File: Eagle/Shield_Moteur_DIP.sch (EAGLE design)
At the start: 25 parts, among them IC1 L6205N

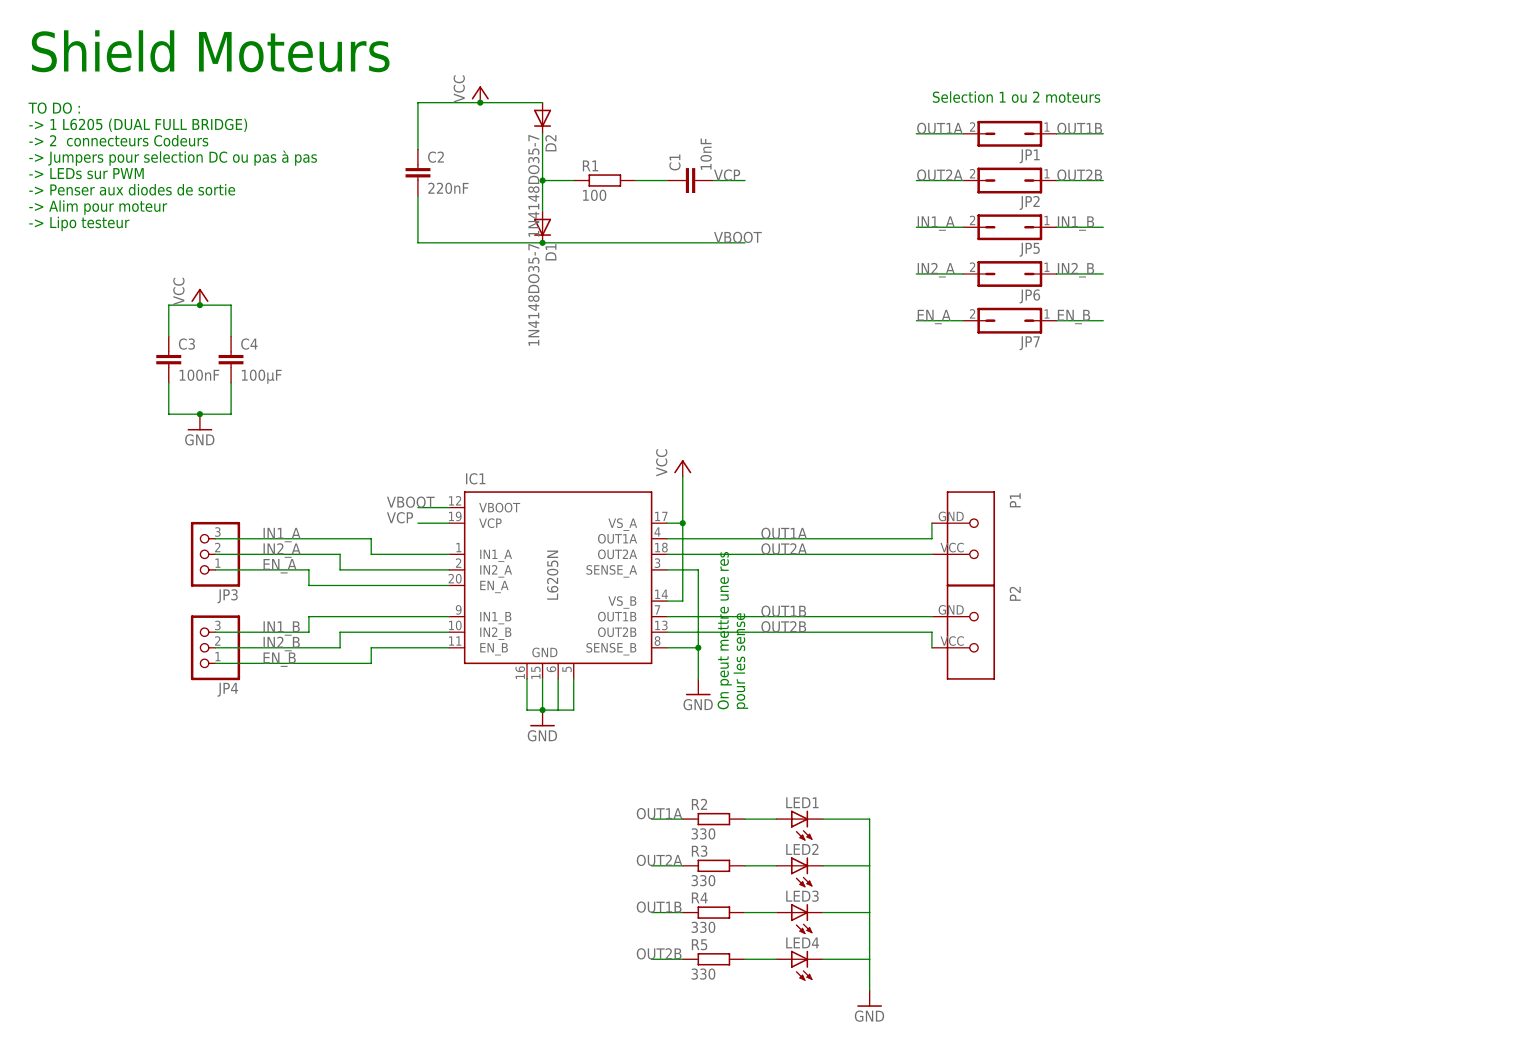
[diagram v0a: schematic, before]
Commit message: Base dsPIC v1.1 & Shield Moteur sans connecteur
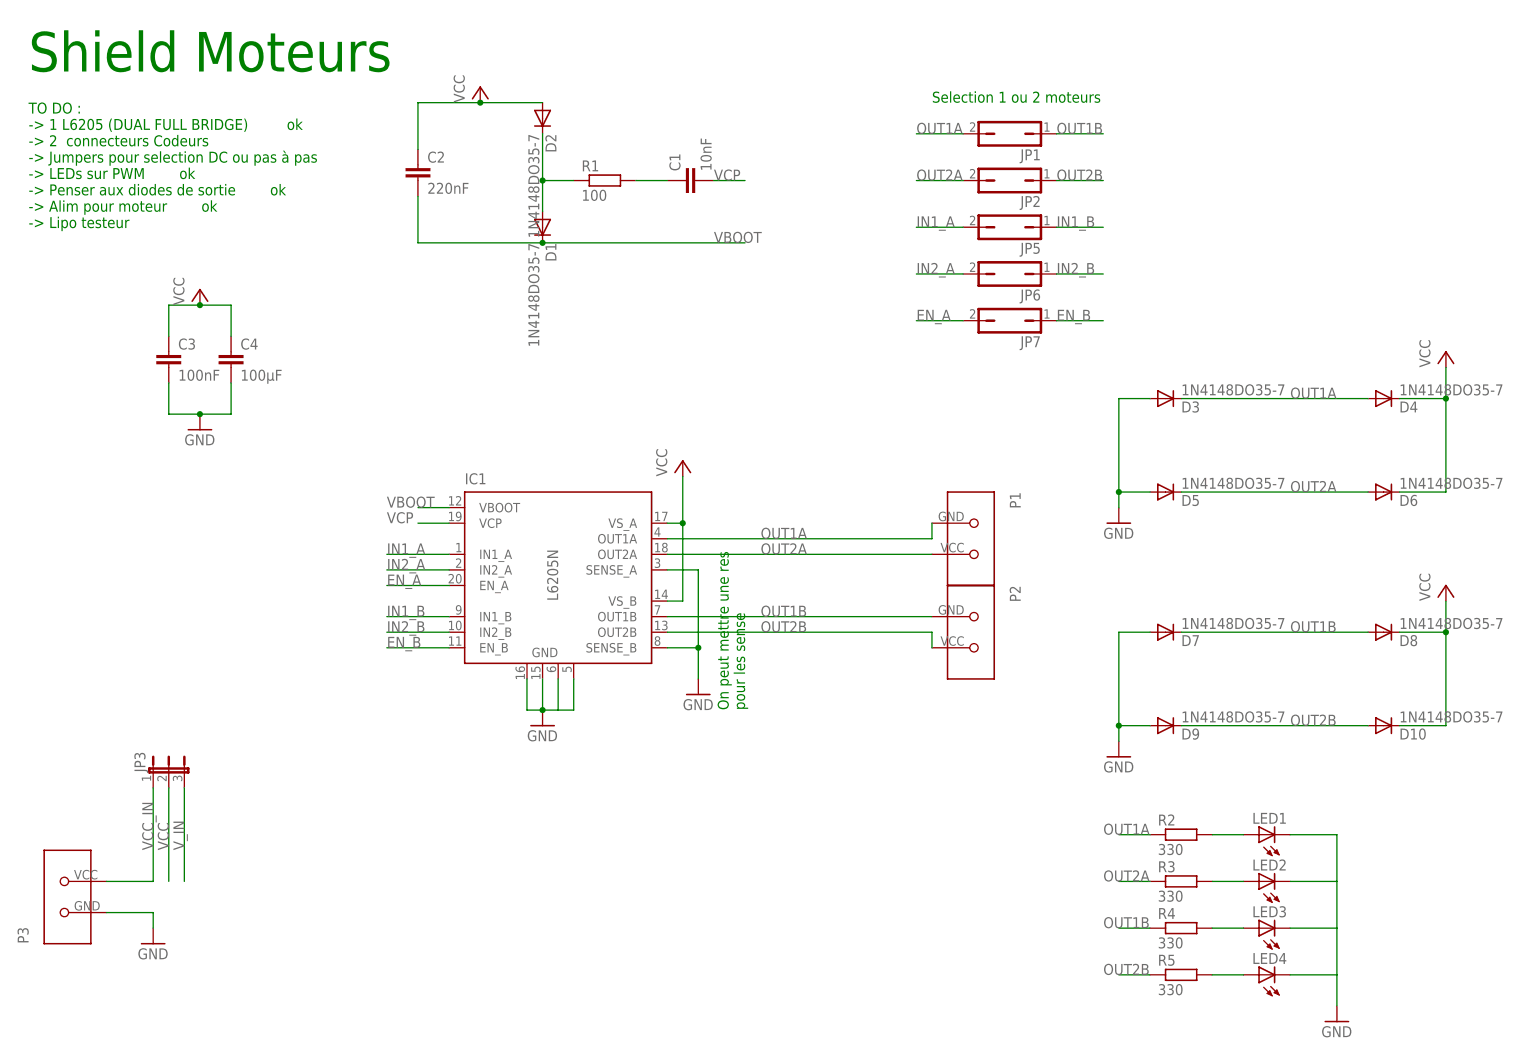
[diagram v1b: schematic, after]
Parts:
- removed JP4: (no value), pinhead:PINHD-1X3
- added D10, D3, D4, D5, D6, D7, D8, D9: 1N4148DO35-7, diode:1N4148DO35-7
- added P3: (no value), Perso:BORNIER_3.5MM
- JP3: device pinhead:PINHD-1X3 -> jumper:JP2E
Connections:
- new net VCC_IN: JP3.1, P3.VCC
- new net V_IN: JP3.3
- net EN_A: no longer JP3.1
- net EN_B: no longer JP4.1
- net GND: now also D3.A, D5.A, D7.A, D9.A, P3.GND
- net IN1_A: no longer JP3.3
- net IN1_B: no longer JP4.3
- net IN2_A: no longer JP3.2
- net IN2_B: no longer JP4.2
- net OUT1A: now also D3.C, D4.A
- net OUT1B: now also D7.C, D8.A
- net OUT2A: now also D5.C, D6.A
- net OUT2B: now also D10.A, D9.C
- net VCC: now also D10.C, D4.C, D6.C, D8.C, JP3.2
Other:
- note added: "TO DO : -> 1 L6205 (DUAL FULL BRIDGE) ok -> 2 connecteurs Codeurs -> Jumpers pour selection DC ou pas à pas -> LEDs sur PWM ok -> Penser aux diodes de sortie ok -> Alim pour moteur ok -> Lipo testeur"
- note removed: "TO DO : -> 1 L6205 (DUAL FULL BRIDGE) -> 2 connecteurs Codeurs -> Jumpers pour selection DC ou pas à pas -> LEDs sur PWM -> Penser aux diodes de sortie -> Alim pour moteur -> Lipo testeur"
- moved on the sheet: LED1, LED2, LED3, LED4, R2, R3, R4, R5
